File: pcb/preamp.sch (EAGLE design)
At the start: 50 parts, among them U1 LT1097CN8PBF, U2 LT1097CN8PBF, U3 LT1079CNPBF, U4 LT1079CNPBF

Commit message: some circuit modifications, updates
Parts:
- R1, R3: value 470 -> 3.3k
- R2, R4: value 3.3k -> 470
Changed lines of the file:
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@@
 <?xml version="1.0" encoding="utf-8"?>
 <!DOCTYPE eagle SYSTEM "eagle.dtd">
-<eagle version="6.6.0">
+<eagle version="7.3.0">
 <drawing>
 <settings>
@@
 <part name="SUPPLY6" library="supply2" deviceset="+10V" device=""/>
 <part name="GND1" library="supply1" deviceset="GND" device=""/>
-<part name="R1" library="resistor" deviceset="R-US_" device="0204/5" value="470"/>
-<part name="R2" library="resistor" deviceset="R-US_" device="0204/5" value="3.3k"/>
-<part name="R3" library="resistor" deviceset="R-US_" device="0204/5" value="470"/>
-<part name="R4" library="resistor" deviceset="R-US_" device="0204/5" value="3.3k"/>
+<part name="R1" library="resistor" deviceset="R-US_" device="0204/5" value="3.3k"/>
+<part name="R2" library="resistor" deviceset="R-US_" device="0204/5" value="470"/>
+<part name="R3" library="resistor" deviceset="R-US_" device="0204/5" value="3.3k"/>
+<part name="R4" library="resistor" deviceset="R-US_" device="0204/5" value="470"/>
 <part name="R8" library="resistor" deviceset="R-US_" device="0204/5" value="1.6k"/>
 <part name="R9" library="resistor" deviceset="R-US_" device="0204/5" value="16.2k"/>
@@
 <net name="1FILTERC" class="0">
 <segment>
-<label x="154.94" y="87.376" size="1.778" layer="95" rot="R180" xref="yes"/>
+<label x="154.94" y="84.836" size="1.778" layer="95" rot="R180" xref="yes"/>
 <pinref part="U3" gate="A" pin="-IN_D"/>
-<wire x1="170.18" y1="83.82" x2="154.94" y2="87.376" width="0.1524" layer="91"/>
+<wire x1="170.18" y1="83.82" x2="154.94" y2="84.836" width="0.1524" layer="91"/>
 </segment>
 <segment>
@@
 <net name="OFFSET" class="0">
 <segment>
-<label x="154.94" y="83.82" size="1.778" layer="95" rot="R180" xref="yes"/>
+<label x="154.94" y="88.9" size="1.778" layer="95" rot="R180" xref="yes"/>
 <pinref part="U3" gate="A" pin="+IN_D"/>
-<wire x1="170.18" y1="86.36" x2="154.94" y2="83.82" width="0.1524" layer="91"/>
-</segment>
-<segment>
+<wire x1="170.18" y1="86.36" x2="154.94" y2="88.9" width="0.1524" layer="91"/>
+</segment>
+<segment>

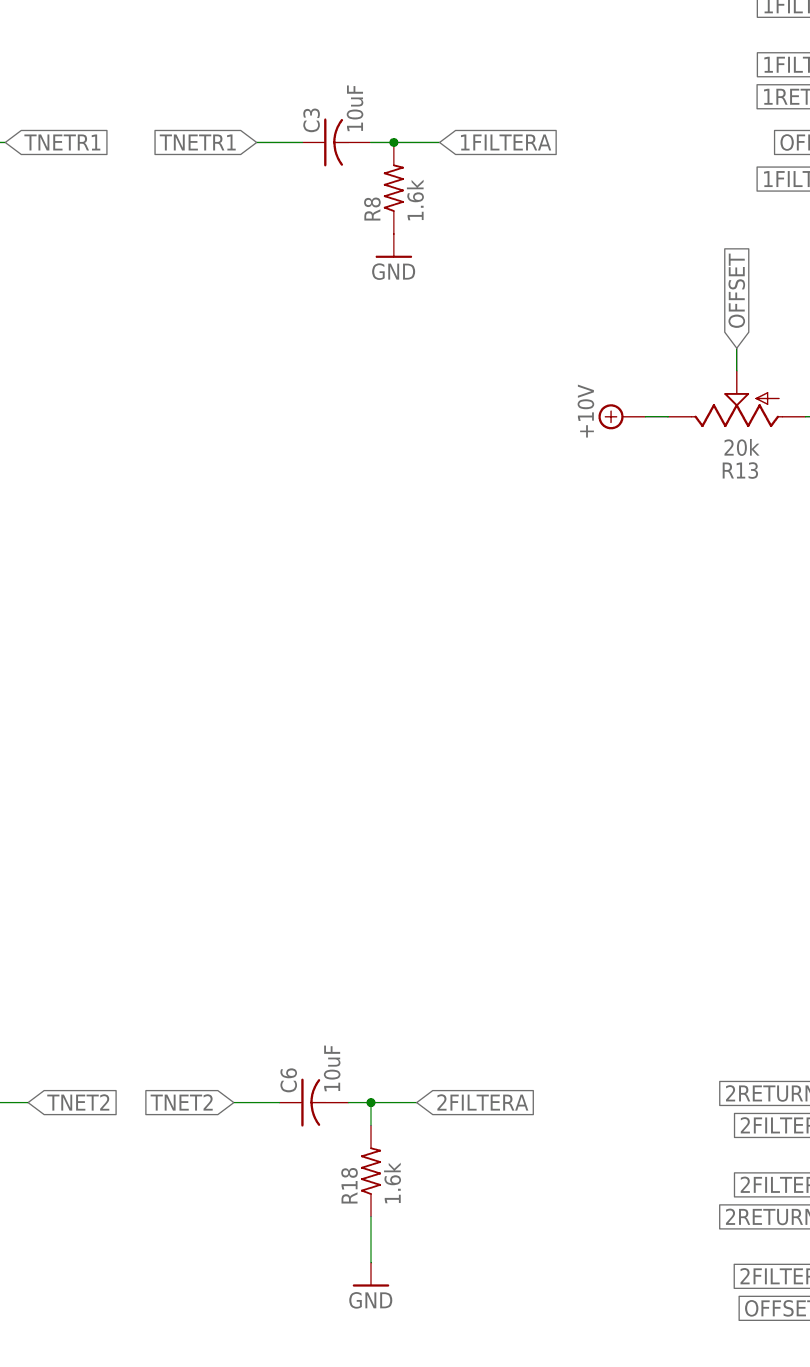
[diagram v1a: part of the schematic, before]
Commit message: playing with simulation, updating component values accordingly
decreasing distortion
component values in the simulation are now more correct.
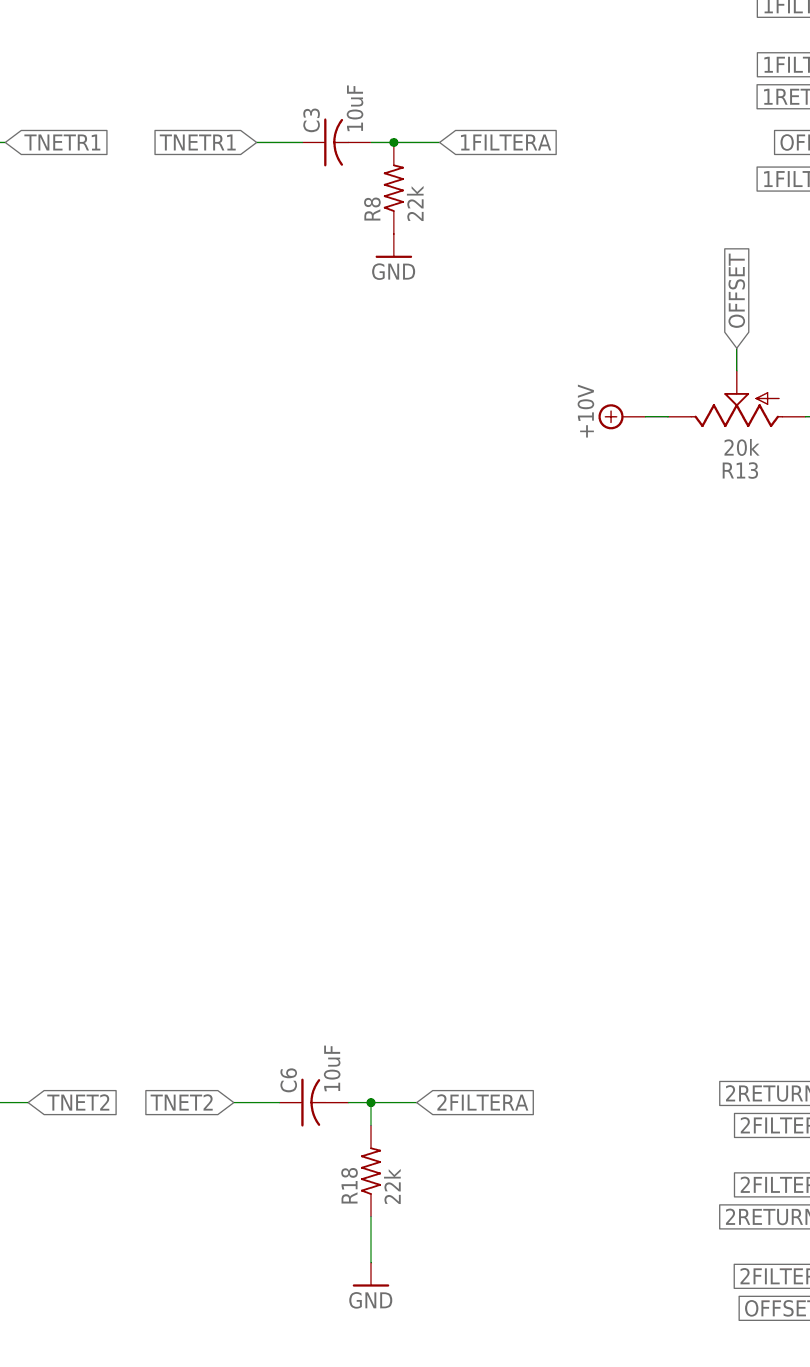
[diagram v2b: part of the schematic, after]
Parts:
- R18, R8: value 1.6k -> 22k
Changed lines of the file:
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@@
 <part name="R3" library="resistor" deviceset="R-US_" device="0204/5" value="3.3k"/>
 <part name="R4" library="resistor" deviceset="R-US_" device="0204/5" value="470"/>
-<part name="R8" library="resistor" deviceset="R-US_" device="0204/5" value="1.6k"/>
+<part name="R8" library="resistor" deviceset="R-US_" device="0204/5" value="22k"/>
 <part name="R9" library="resistor" deviceset="R-US_" device="0204/5" value="16.2k"/>
 <part name="R10" library="resistor" deviceset="R-US_" device="0204/5" value="7.9k"/>
@@
 <part name="SUPPLY12" library="supply2" deviceset="-10V" device=""/>
 <part name="C6" library="resistor" deviceset="C-US" device="050-030X075" value="10uF"/>
-<part name="R18" library="resistor" deviceset="R-US_" device="0204/5" value="1.6k"/>
+<part name="R18" library="resistor" deviceset="R-US_" device="0204/5" value="22k"/>
 <part name="GND8" library="supply1" deviceset="GND" device=""/>
 <part name="R19" library="resistor" deviceset="R-US_" device="0204/5" value="7.9k"/>

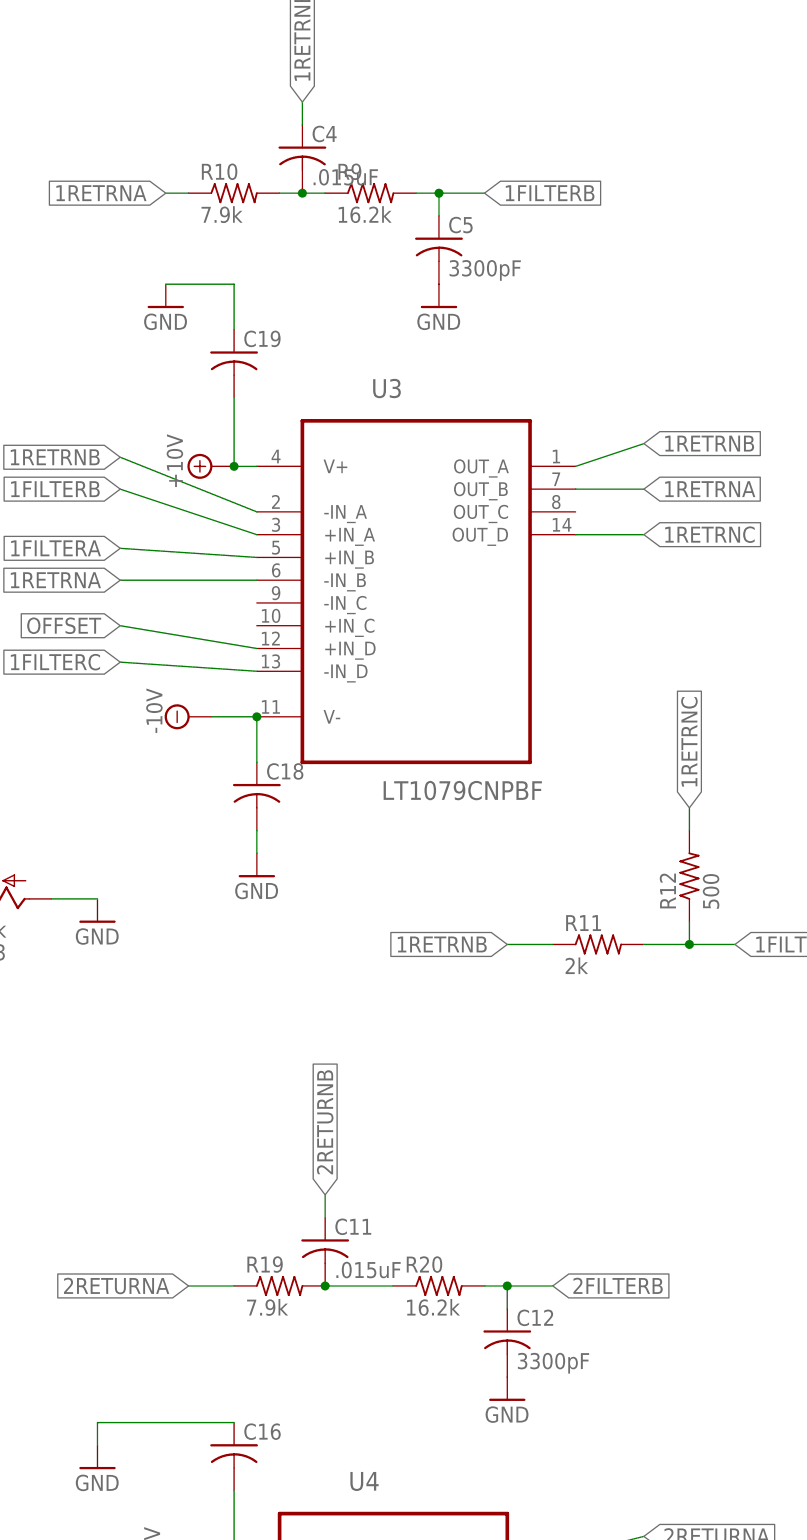
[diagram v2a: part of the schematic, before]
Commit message: updating schematic to reflect new component values
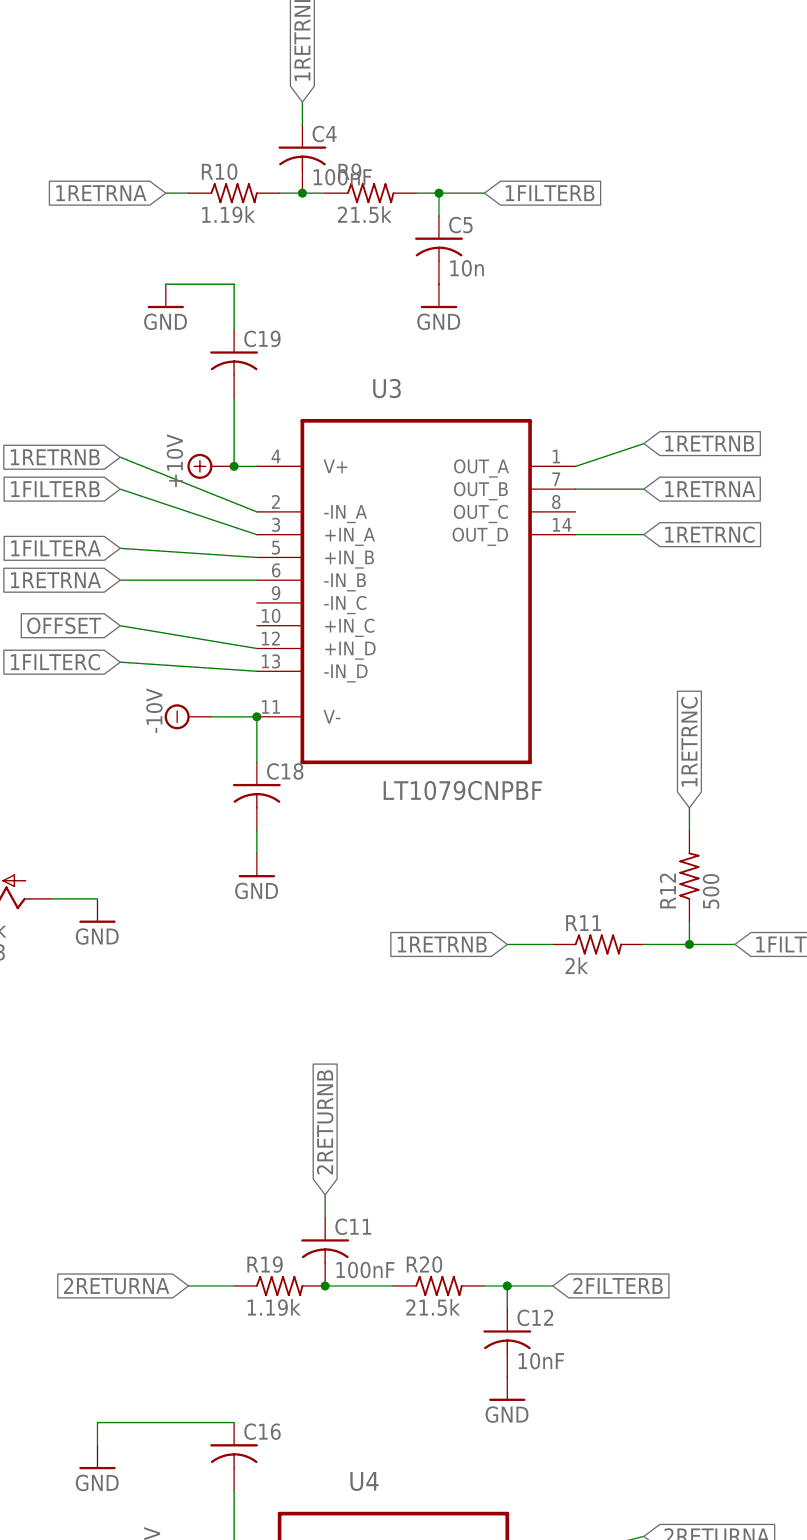
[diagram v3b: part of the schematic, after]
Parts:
- C11, C4: value .015uF -> 100nF
- C12: value 3300pF -> 10nF
- C5: value 3300pF -> 10n
- R10, R19: value 7.9k -> 1.19k
- R20, R9: value 16.2k -> 21.5k
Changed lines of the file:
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@@
 <part name="R4" library="resistor" deviceset="R-US_" device="0204/5" value="470"/>
 <part name="R8" library="resistor" deviceset="R-US_" device="0204/5" value="22k"/>
-<part name="R9" library="resistor" deviceset="R-US_" device="0204/5" value="16.2k"/>
-<part name="R10" library="resistor" deviceset="R-US_" device="0204/5" value="7.9k"/>
+<part name="R9" library="resistor" deviceset="R-US_" device="0204/5" value="21.5k"/>
+<part name="R10" library="resistor" deviceset="R-US_" device="0204/5" value="1.19k"/>
 <part name="R5" library="resistor" deviceset="R-US_" device="0204/7" value="560k"/>
 <part name="R6" library="resistor" deviceset="R-US_" device="0204/7" value="560k"/>
@@
 <part name="C3" library="resistor" deviceset="C-US" device="050-030X075" value="10uF"/>
 <part name="GND4" library="supply1" deviceset="GND" device=""/>
-<part name="C4" library="resistor" deviceset="C-US" device="050-024X044" value=".015uF"/>
-<part name="C5" library="resistor" deviceset="C-US" device="025-024X044" value="3300pF"/>
+<part name="C4" library="resistor" deviceset="C-US" device="050-024X044" value="100nF"/>
+<part name="C5" library="resistor" deviceset="C-US" device="025-024X044" value="10n"/>
 <part name="GND5" library="supply1" deviceset="GND" device=""/>
 <part name="R11" library="resistor" deviceset="R-US_" device="0204/5" value="2k"/>
@@
 <part name="R18" library="resistor" deviceset="R-US_" device="0204/5" value="22k"/>
 <part name="GND8" library="supply1" deviceset="GND" device=""/>
-<part name="R19" library="resistor" deviceset="R-US_" device="0204/5" value="7.9k"/>
-<part name="C11" library="resistor" deviceset="C-US" device="050-024X044" value=".015uF"/>
-<part name="R20" library="resistor" deviceset="R-US_" device="0204/5" value="16.2k"/>
-<part name="C12" library="resistor" deviceset="C-US" device="025-024X044" value="3300pF"/>
+<part name="R19" library="resistor" deviceset="R-US_" device="0204/5" value="1.19k"/>
+<part name="C11" library="resistor" deviceset="C-US" device="050-024X044" value="100nF"/>
+<part name="R20" library="resistor" deviceset="R-US_" device="0204/5" value="21.5k"/>
+<part name="C12" library="resistor" deviceset="C-US" device="025-024X044" value="10nF"/>
 <part name="GND9" library="supply1" deviceset="GND" device=""/>
 <part name="R21" library="resistor" deviceset="R-US_" device="0204/5" value="2k"/>
